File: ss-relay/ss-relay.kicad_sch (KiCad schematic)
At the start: 8 parts, among them J1 Conn_01x01, K1 G5Q-1EU DC12, Q1 SiS413DNT, Q2 SiS413DNT

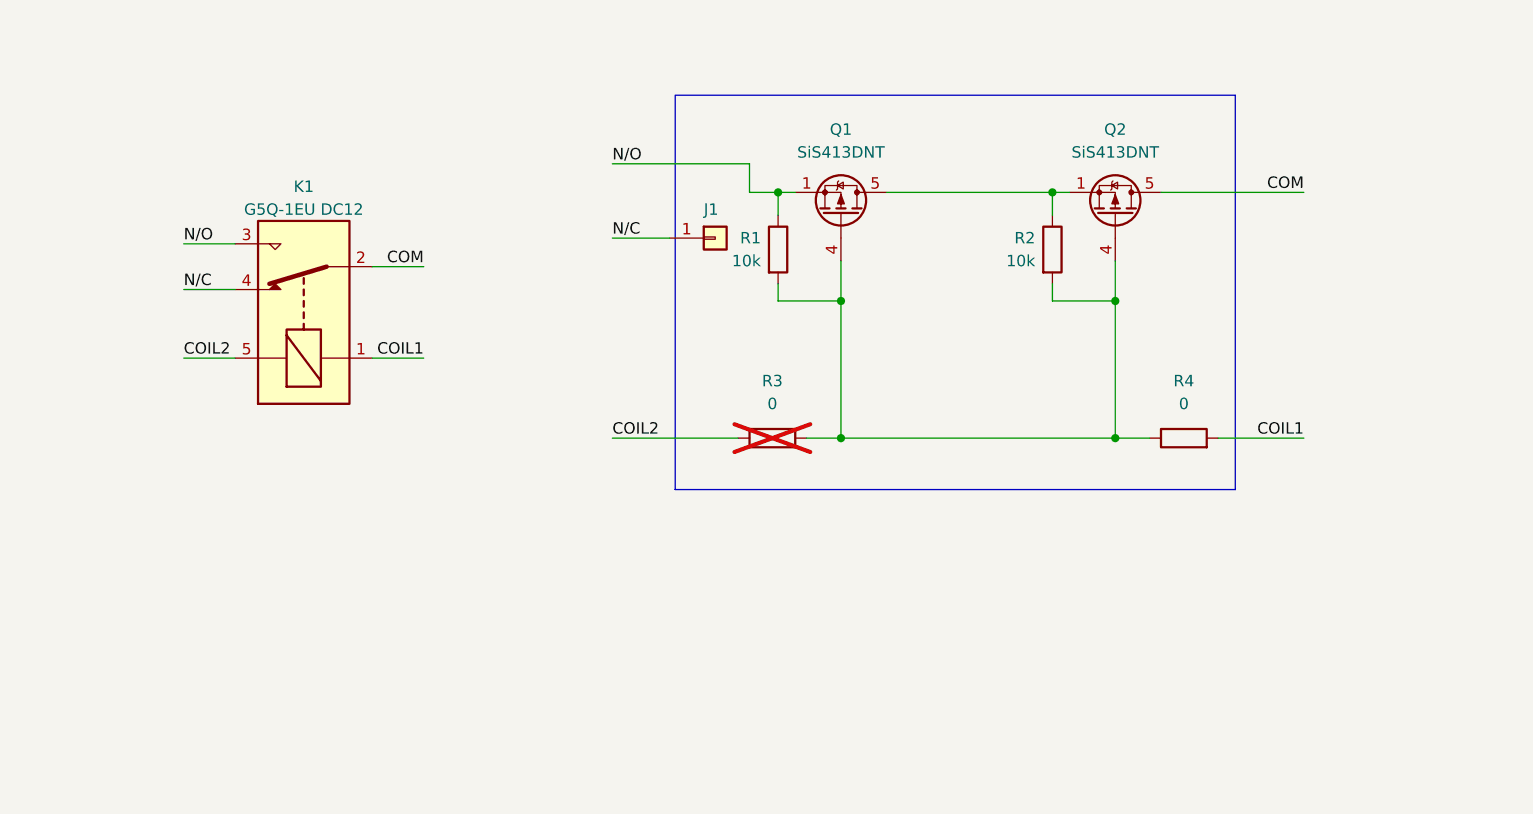
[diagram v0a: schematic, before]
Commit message: Commented schematics; generated BOMs
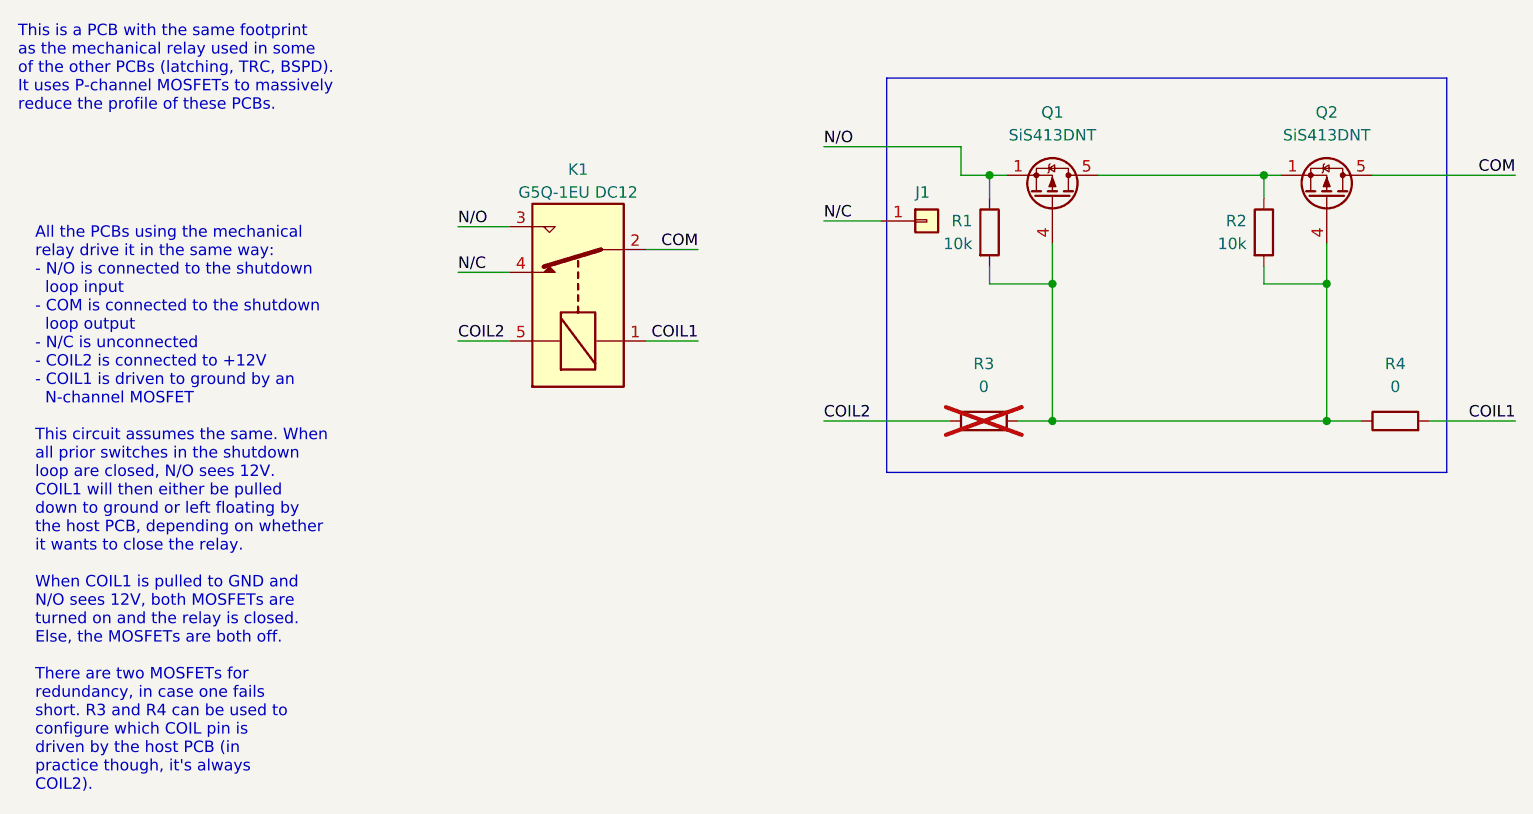
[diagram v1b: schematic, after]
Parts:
- Q1, Q2: Order Code (none) -> 78-SIS413DN-T1-GE3; Supplier (none) -> Mouser
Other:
- note added: "All the PCBs using the mechanical relay drive it in the same way: - N/O is connected to the shutdown loop input - COM is connected to the shutdown loop output - N/C is unconnected - COIL2 is connected to +12V - COIL1 is driven to ground by an N-channel MOSFET This circuit assumes the same. When all prior switches in the shutdown loop are closed, N/O sees 12V. COIL1 will then either be pulled down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"
- note added: "This is a PCB with the same footprint as the mechanical relay used in some of the other PCBs (latching, TRC, BSPD). It uses P-channel MOSFETs to massively reduce the profile of these PCBs."
- moved on the sheet: J1, K1, Q1, Q2, R1, R2, R3, R4
